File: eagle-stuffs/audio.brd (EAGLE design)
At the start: 57.1 x 44.5 mm, 28 parts, among them IC2 TL084P, IC3 DS1804-10k, IC4 DS1804, U1 AT42QT1010SOT23, U2 SSM2211SZ

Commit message: Final beta
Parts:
- removed C7: 0.01, rcl:C025-025X050
- removed C8: 0.1, rcl:C025-025X050
- removed R1: 10k, resistor:0207/10
- removed U1: AT42QT1010SOT23, SparkFun-DigitalIC:SOT23-6
- R4: value 15K -> 15k
- R5: value 10K -> 10k
- R6: value 33K -> 33k
- R7: value 1K -> 1k
- R8, R9: value 100K -> 100k
- TOUCH: device adafruit:1X01 -> adafruit:1X03
- moved IN 51.1 mm to (53.3, 24.1)
- moved R2 37.0 mm to (45.7, 22.9)
- moved TOUCH 25.7 mm to (10.2, 40.6), turned to 0 degrees
- moved R3 21.6 mm to (45.7, 33.0)
- moved R5 13.0 mm to (35.6, 15.2)
- moved R7 13.0 mm to (35.6, 19.1)
- moved R8 12.8 mm to (21.6, 15.2)
- moved SPK 6.48 mm to (53.3, 31.8)
- moved C6 4.02 mm to (44.5, 6.35)
- moved R6 4.02 mm to (44.5, 10.2)
- moved IC3 2.84 mm to (22.9, 27.9)
- moved C3 2.84 mm to (36.8, 33.0)
- moved U2 2.84 mm to (36.8, 27.9)
- moved C2 2.84 mm to (36.8, 22.9)
- moved C1 2.54 mm to (43.2, 27.9)
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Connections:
- removed net N$16: C7.1, R1.2, U1.3
- removed net N$17: C7.2, U1.4
- removed net N$24: CTRL.6, U1.1
- net +5V: now also TOUCH.2; no longer C8.1, U1.5, U1.6
- net GND: now also TOUCH.3; no longer C8.2, U1.2
- net N$22: now also CTRL.6; no longer R1.1
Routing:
- net GND: track 0.00 -> 141.0 mm
- net +5V: track 0.00 -> 115.9 mm
- net N$1: track 0.00 -> 56.5 mm
- net N$11: track 0.00 -> 49.5 mm
- net N$14: track 0.00 -> 46.8 mm
- net N$20: track 0.00 -> 41.5 mm
- net N$10: track 0.00 -> 34.1 mm
- net N$8: track 0.00 -> 33.8 mm
- net VCC: track 0.00 -> 33.8 mm
- net N$15: track 0.00 -> 33.0 mm
- net N$21: track 0.00 -> 31.6 mm
- net N$4: track 0.00 -> 28.3 mm
- net N$2: track 0.00 -> 28.0 mm
- net N$19: track 0.00 -> 25.1 mm
- net N$6: track 0.00 -> 22.4 mm
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- added copper zone on layer 1, net GND
- added copper zone on layer 16, net N$16

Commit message: Minor stuffs
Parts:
- removed R2: 8k, resistor:0207/10
- IC3: value DS1804-10k -> DS1804-50k
- IC4: value DS1804 -> DS1804-100k
- R3: value 10k -> 20k
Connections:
- removed net N$7: IC3.5, R2.1
- net N$4: now also IC3.5; no longer R2.2
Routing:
- net N$7: track 18.2 -> 0.00 mm, vias 1 -> 0
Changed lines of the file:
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@@
 <attribute name="VALUE" x="34.671" y="8.255" size="1.27" layer="27" ratio="10" rot="R180"/>
 </element>
-<element name="IC3" library="pot-xicor" package="DIL08" value="DS1804-10k" x="22.86" y="27.94" smashed="yes">
+<element name="IC3" library="pot-xicor" package="DIL08" value="DS1804-50k" x="22.86" y="27.94" smashed="yes">
 <attribute name="OC_NEWARK" value="51J6928" x="22.86" y="27.94" size="1.778" layer="27" display="off"/>
 <attribute name="MPN" value="X9C102P" x="22.86" y="27.94" size="1.778" layer="27" display="off"/>
@@
 <attribute name="VALUE" x="19.304" y="27.305" size="1.27" layer="27" ratio="10"/>
 </element>
-<element name="IC4" library="pot-xicor" package="DIL08" value="DS1804" x="8.89" y="27.94" smashed="yes">
+<element name="IC4" library="pot-xicor" package="DIL08" value="DS1804-100k" x="8.89" y="27.94" smashed="yes">
 <attribute name="OC_NEWARK" value="51J6928" x="8.89" y="27.94" size="1.778" layer="27" display="off"/>
 <attribute name="MPN" value="X9C102P" x="8.89" y="27.94" size="1.778" layer="27" display="off"/>
@@
 <attribute name="NAME" x="3.556" y="25.019" size="1.27" layer="25" ratio="10" rot="R90"/>
 <attribute name="VALUE" x="5.334" y="27.305" size="1.27" layer="27" ratio="10"/>
-</element>
-<element name="R2" library="resistor" package="0207/10" value="8k" x="45.72" y="22.86" smashed="yes">
-<attribute name="NAME" x="45.212" y="21.844" size="1.27" layer="25" ratio="10"/>
-<attribute name="VALUE" x="43.4594" y="22.225" size="1.27" layer="27" ratio="10"/>
 </element>
 <element name="R10" library="resistor" package="0207/10" value="1k" x="8.89" y="19.05" smashed="yes">
@@
 <attribute name="VALUE" x="31.115" y="31.3944" size="2.0828" layer="27" ratio="10" rot="SR270"/>
 </element>
-<element name="R3" library="resistor" package="0207/10" value="10k" x="45.72" y="33.02" smashed="yes">
+<element name="R3" library="resistor" package="0207/10" value="20k" x="45.72" y="33.02" smashed="yes">
 <attribute name="NAME" x="43.942" y="32.004" size="1.27" layer="25" ratio="10"/>
 <attribute name="VALUE" x="43.4594" y="32.385" size="1.27" layer="27" ratio="10"/>
@@
 <contactref element="U2" pad="4"/>
 <contactref element="R3" pad="1"/>
-<contactref element="R2" pad="2"/>
 <wire x1="34.281" y1="30.472" x2="34.867" y2="30.472" width="0.381" layer="1"/>
 <wire x1="33.402" y1="31.351" x2="34.281" y2="30.472" width="0.381" layer="1"/>
@@
 <wire x1="41.606" y1="31.644" x2="43.071" y2="31.644" width="0.381" layer="16"/>
 <wire x1="40.434" y1="32.816" x2="41.606" y2="31.644" width="0.381" layer="16"/>
-<wire x1="50.689" y1="23.147" x2="50.8" y2="22.86" width="0.381" layer="16"/>
 <wire x1="40.434" y1="32.816" x2="40.64" y2="33.02" width="0.381" layer="16"/>
+<contactref element="IC3" pad="5"/>
+<wire x1="26.67" y1="31.75" x2="33.402" y2="31.351" width="0" layer="19" extent="1-1"/>
 </signal>
 <signal name="N$5">
@@
 <wire x1="53.326" y1="33.109" x2="53.34" y2="33.02" width="0.381" layer="1"/>
 </signal>
-<signal name="N$7">
-<contactref element="IC3" pad="5"/>
-<contactref element="R2" pad="1"/>
-<wire x1="28.128" y1="31.644" x2="26.956" y2="31.644" width="0.381" layer="1"/>
-<wire x1="33.402" y1="26.37" x2="28.128" y2="31.644" width="0.381" layer="1"/>
-<wire x1="35.16" y1="24.612" x2="33.402" y2="26.37" width="0.381" layer="16"/>
-<wire x1="38.676" y1="24.612" x2="35.16" y2="24.612" width="0.381" layer="16"/>
-<wire x1="40.141" y1="23.147" x2="38.676" y2="24.612" width="0.381" layer="16"/>
-<wire x1="40.141" y1="22.854" x2="40.141" y2="23.147" width="0.381" layer="16"/>
-<wire x1="40.434" y1="22.561" x2="40.141" y2="22.854" width="0.381" layer="16"/>
-<wire x1="40.727" y1="22.854" x2="40.434" y2="22.561" width="0.381" layer="16"/>
-<wire x1="26.956" y1="31.644" x2="26.67" y2="31.75" width="0.381" layer="1"/>
-<wire x1="40.727" y1="22.854" x2="40.64" y2="22.86" width="0.381" layer="16"/>
-<via x="33.402" y="26.37" extent="1-16" drill="0.3302"/>
-</signal>
 <signal name="N$18">

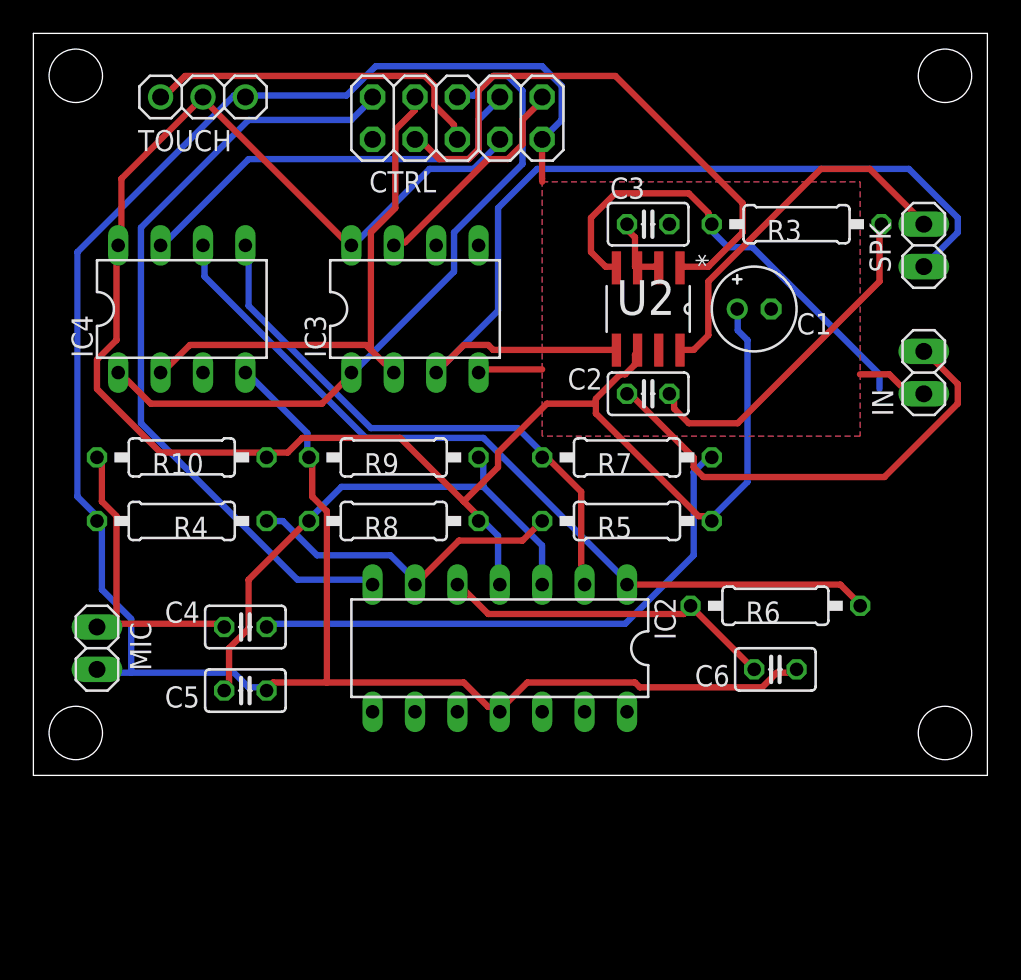
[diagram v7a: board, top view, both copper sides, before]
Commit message: Changed some drilling size
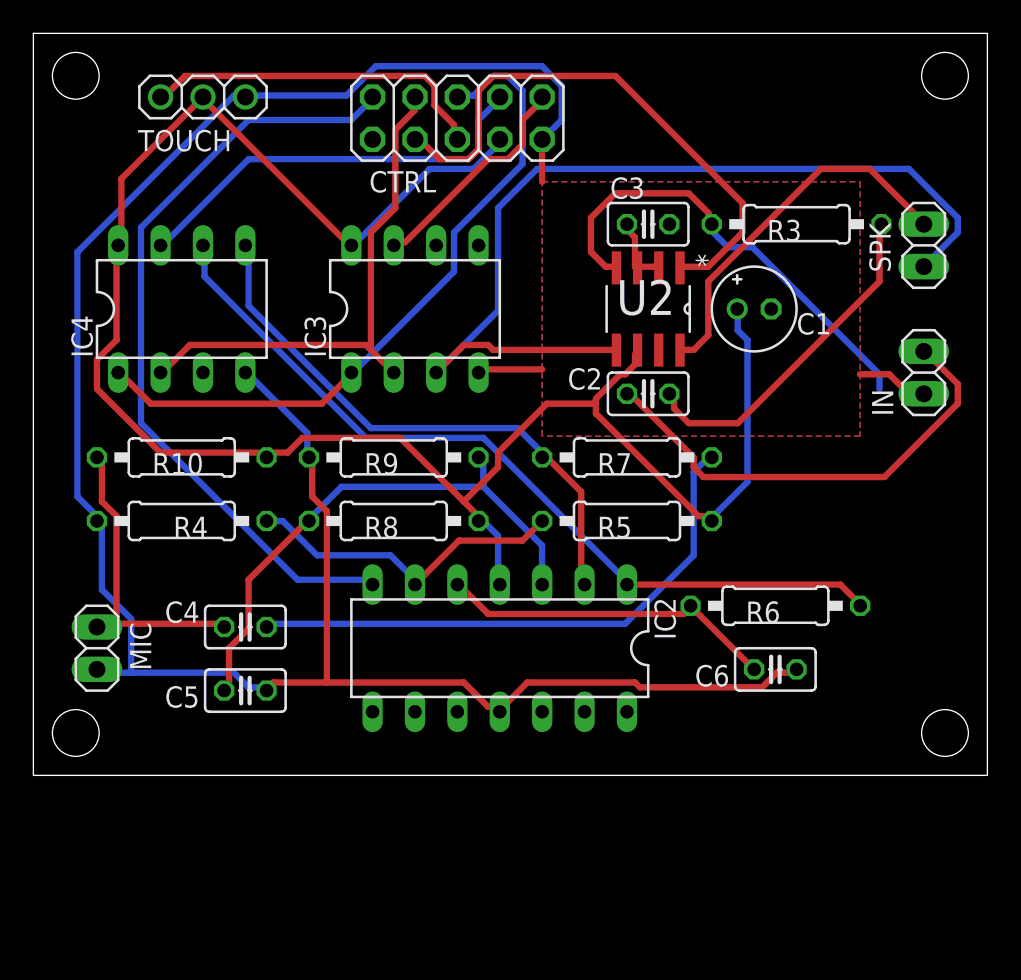
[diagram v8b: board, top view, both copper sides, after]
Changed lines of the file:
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@@
 <wire x1="57.15" y1="44.45" x2="57.15" y2="0" width="0" layer="20"/>
 <wire x1="57.15" y1="0" x2="0" y2="0" width="0" layer="20"/>
-<hole x="2.54" y="2.54" drill="3.2"/>
-<hole x="2.54" y="41.91" drill="3.2"/>
-<hole x="54.61" y="41.91" drill="3.2"/>
-<hole x="54.61" y="2.54" drill="3.2"/>
+<hole x="2.54" y="2.54" drill="2.8"/>
+<hole x="2.54" y="41.91" drill="2.8"/>
+<hole x="54.61" y="41.91" drill="2.8"/>
+<hole x="54.61" y="2.54" drill="2.8"/>
 <rectangle x1="34.29" y1="26.67" x2="39.37" y2="29.21" layer="41"/>
 </plain>
